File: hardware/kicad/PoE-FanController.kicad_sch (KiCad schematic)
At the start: 31 parts, among them J2 FAN1, J3 FAN2, J4 FAN3, J5 FAN4, J6 Molex_KK254_3pin, J8 Waveshare_ESP32P4POEETH, U1 LM2587-12

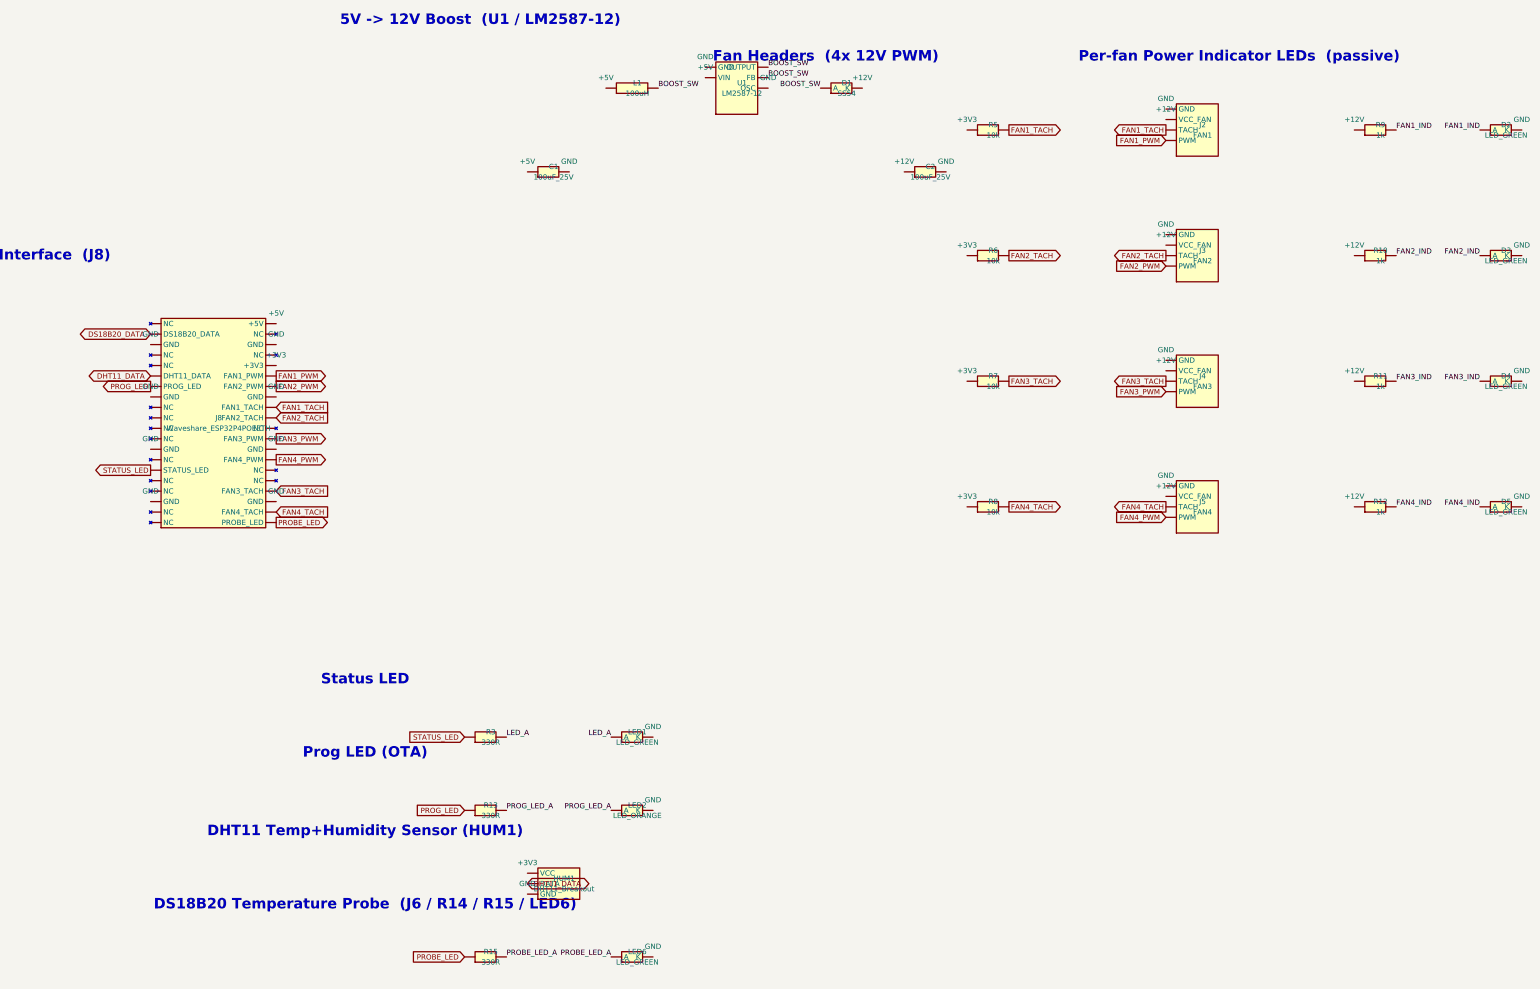
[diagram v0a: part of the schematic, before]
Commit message: hw(sch): overhaul pin assignments and rename signals per user spec
Signal changes (v0.6):
  Left column (all sensors/indicators now on left):
  - Pin 6  DS18B20_DATA (GPIO2)  was: STATUS_LED
  - Pin 7  PROBE_LED    (GPIO3)  was: NC
  - Pin 14 DHT11_DATA  (GPIO15)  was: PROG_LED
  - Pin 16 PROG_LED    (GPIO17)  was: NC
  - Pin 17 PWR_LED     (GPIO18)  renamed from STATUS_LED, was NC
  - Pin 19 NC (was DS18B20_DATA/GPIO19)
  - Pin 15 NC (was DHT11_DATA/GPIO16)

  Right column (fan signals only):
  - Pin 21 FAN4_TACH  (GPIO48)   was: PROBE_LED
  - Pin 22 FAN4_PWM   (GPIO47)   was: FAN4_TACH
  - Pin 26 FAN3_TACH  (GPIO32)   was: NC (note: verify EMAC not active)
  - Pin 27 FAN3_PWM   (GPIO27)   was: FAN4_PWM
  - Pin 32 FAN2_PWM   (GPIO22)   was: FAN1_TACH
  - Pin 34 FAN1_TACH  (GPIO21)   was: FAN2_PWM
  - Pins 24,29,31,35 now NC (GPIO46,GPIO26,GPIO23,GPIO20 unused)

Fan header assignments:
  - J2 (FAN1): TACH only (no PWM — full speed), pull-up R5
  - J3 (FAN2): PWM only (no TACH monitoring), no pull-up
  - J4 (FAN3): PWM + TACH, pull-up R7
  - J5 (FAN4): PWM + TACH, pull-up R8
  - R6 removed (FAN2 has no TACH)

Schematic cleanup:
  - Removed per-fan passive indicator LEDs (D2-D5, R9-R12) — reduces noise
  - PROBE_LED circuit now adjacent to J6/DS18B20 section in schematic
  - PWR_LED (was STATUS_LED) clearly named and documented

ERC: 0 errors (54 pre-existing lib_symbol_mismatch warnings)

Co-authored-by: Copilot <223556219+Copilot@users.noreply.github.com>
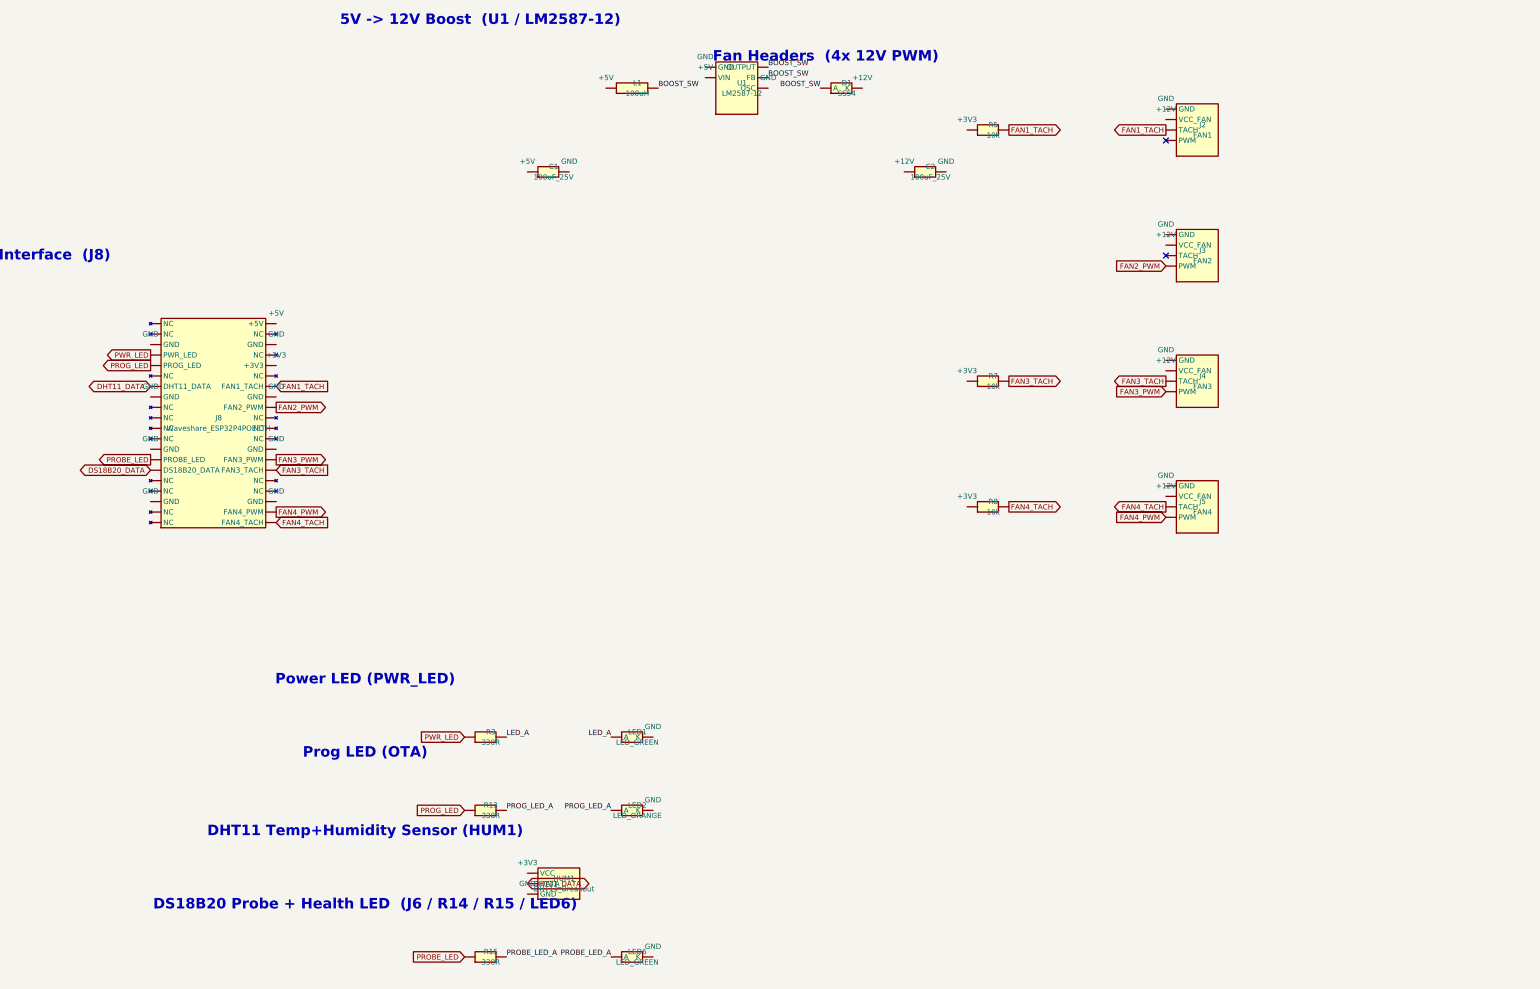
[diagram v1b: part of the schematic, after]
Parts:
- removed D3, D4, D5: LED_GREEN, LED_THT:LED_D3.0mm, symbol Custom:LED_SMD
- removed R10, R11, R12, R9: 1k, Resistor_THT:R_Axial_DIN0207_L6.3mm_D2.5mm_P7.62mm_Horizontal, symbol Custom:R
- removed R13: 330R, Resistor_THT:R_Axial_DIN0207_L6.3mm_D2.5mm_P7.62mm_Horizontal, symbol Custom:R
- removed R6: 10k, Resistor_THT:R_Axial_DIN0207_L6.3mm_D2.5mm_P7.62mm_Horizontal, symbol Custom:R
- R13: renamed from D2; value LED_GREEN -> 330R; footprint LED_THT:LED_D3.0mm -> Resistor_THT:R_Axial_DIN0207_L6.3mm_D2.5mm_P7.62mm_Horizontal; symbol Custom:LED_SMD -> Custom:R
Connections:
- net FAN1_IND is gone; now on net PROG_LED: R13.1
- net DHT11_DATA: now also J8.14 (DHT11_DATA); no longer J8.15 (DHT11_DATA)
- net DS18B20_DATA: now also J8.6 (DS18B20_DATA); no longer J8.19 (DS18B20_DATA)
- net FAN1_TACH: now also J8.34 (FAN1_TACH); no longer J8.32 (FAN1_TACH)
- net FAN2_PWM: now also J8.32 (FAN2_PWM); no longer J8.34 (FAN2_PWM)
- net FAN3_PWM: now also J8.27 (FAN3_PWM); no longer J8.29 (FAN3_PWM)
- net FAN3_TACH: now also J8.26 (FAN3_TACH); no longer J8.24 (FAN3_TACH)
- net FAN4_PWM: now also J8.22 (FAN4_PWM); no longer J8.27 (FAN4_PWM)
- net FAN4_TACH: now also J8.21 (FAN4_TACH); no longer J8.22 (FAN4_TACH)
- net PROBE_LED: now also J8.7 (PROBE_LED); no longer J8.21 (PROBE_LED)
- net PROG_LED: now also J8.16 (PROG_LED); no longer J8.14 (PROG_LED)
- net PROG_LED_A: now also R13.2
- net PWR_LED: now reaches J8.17 (PWR_LED)
- net PWR_LED: now also R3.1
- net FAN1_PWM: no longer names the net of J2.4 (PWM)
- net FAN1_PWM: no longer J8.35 (FAN1_PWM)
- net FAN2_TACH: no longer names the net of J3.3 (TACH)
- net FAN2_TACH: no longer J8.31 (FAN2_TACH)
- removed net STATUS_LED: J8.6 (STATUS_LED), R3.1
- no-connect marks 0 -> 2
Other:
- note added: "DS18B20 Probe + Health LED (J6 / R14 / R15 / LED6)"
- note added: "Power LED (PWR_LED)"
- note removed: "DS18B20 Temperature Probe (J6 / R14 / R15 / LED6)"
- note removed: "Per-fan Power Indicator LEDs (passive)"
- note removed: "Status LED"

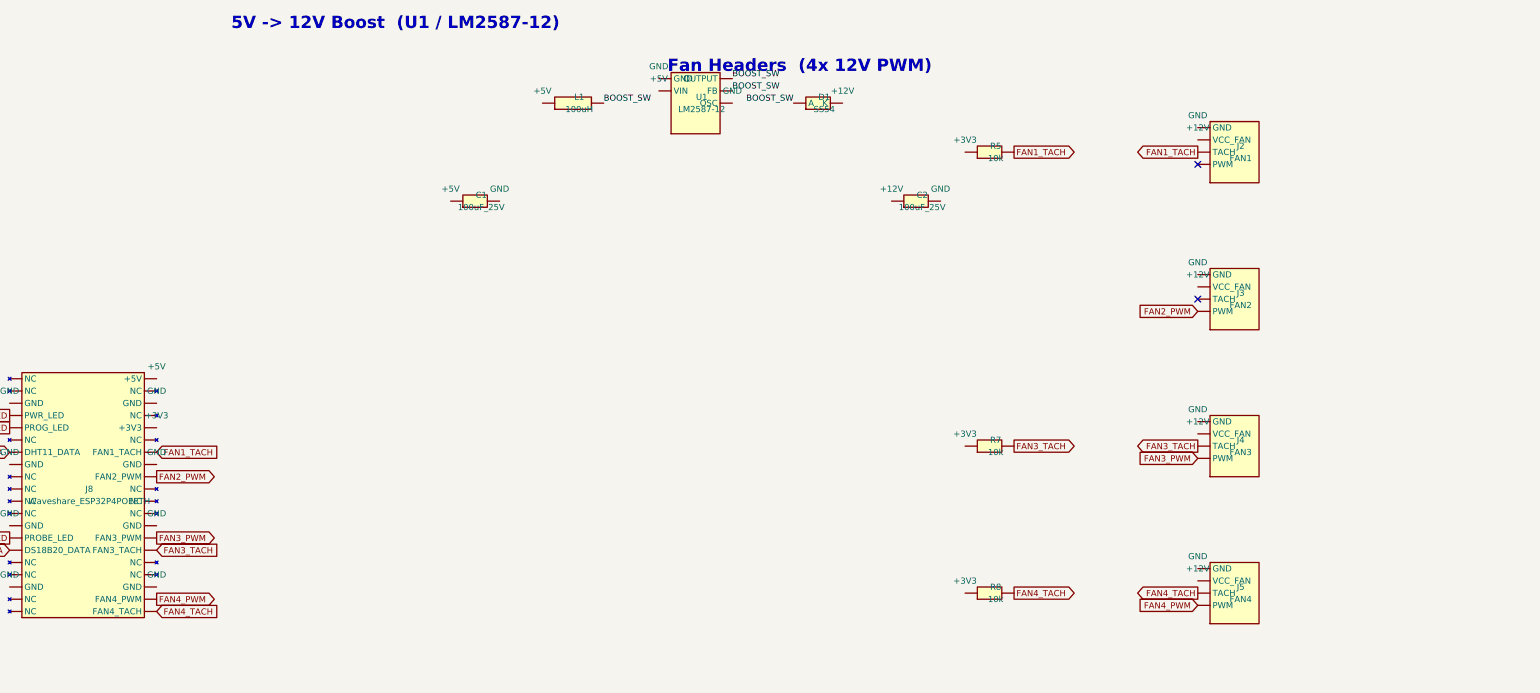
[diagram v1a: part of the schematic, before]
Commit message: hw(sch/pcb): add PWM-driven indicator LEDs (issue #175)
Schematic changes:
- FAN1_PWM re-added on J8 pin 35 (GPIO20) — all 4 fans now have PWM control
- fan_data updated: J2(FAN1_PWM+TACH), J3(FAN2_PWM only), J4/J5(PWM+TACH)
- 4x indicator LED circuits (D2-D5 + R9-R12, 150Ω) added to schematic
  Each LED tapped directly on FAN{n}_PWM signal line:
    FAN{n}_PWM ──[150Ω R]──[LED anode]──[LED cathode]── GND
  LED brightness proportional to PWM duty cycle
- Removed redundant R6 TACH pull-up (FAN2 has no TACH)
- ERC: 0 errors

PCB changes:
- D2-D5 (PWM LEDs) placed at (67, 10/22/34/46) — between J8 and fan headers
- R9-R12 (150Ω resistors) placed at (53, 10/22/34/46)
- R15 (PROBE_LED resistor) moved to (7,50) — left zone above J6
- LED6 (PROBE_LED) moved to (7,44) — directly above J6(DS18B20) as requested
- All pad nets synced to new schematic v0.6 + issue #175

Routing: 125 tracks. Complex DRC conflicts (TACH/+12V interactions, left-zone
signal routing through ESP32 zone) require KiCad GUI for final cleanup.
8 unconnected items and routing shorts need interactive routing session.

Closes #175

Co-authored-by: Copilot <223556219+Copilot@users.noreply.github.com>
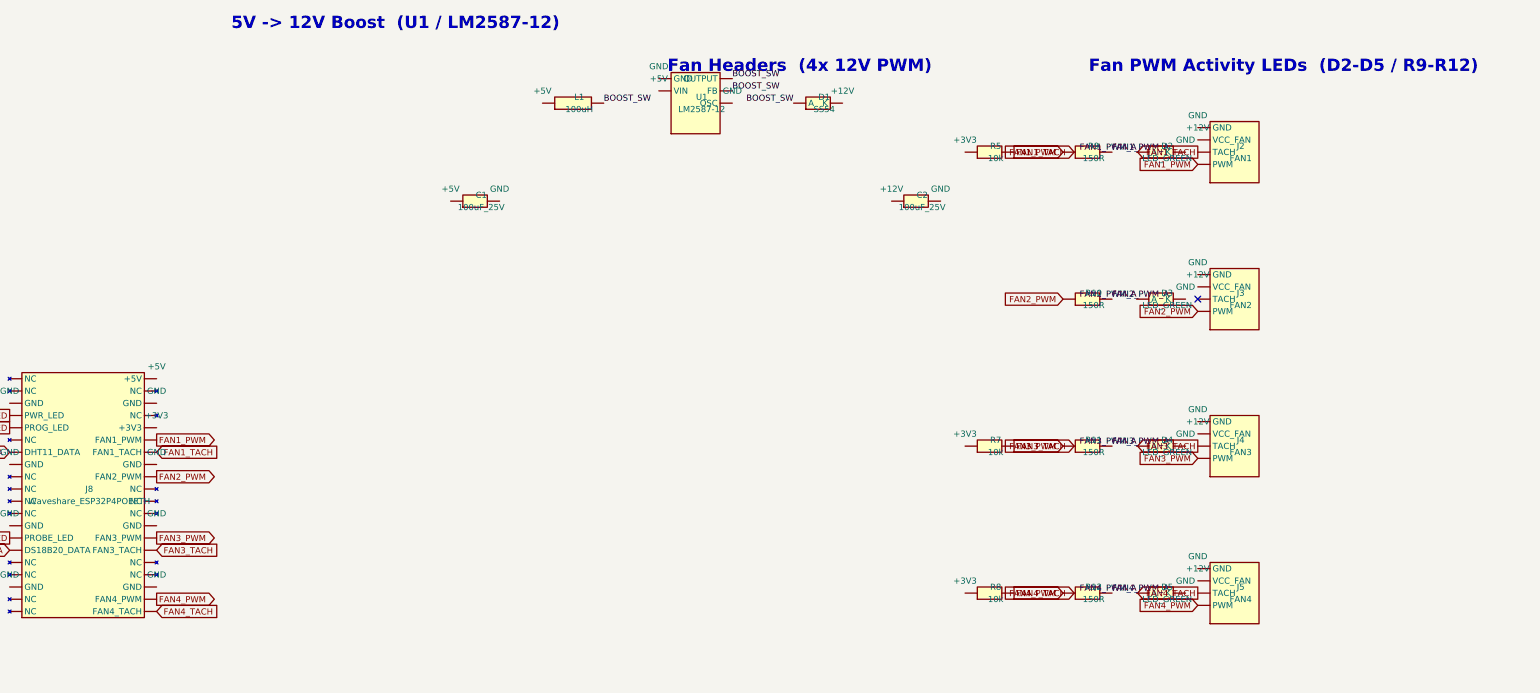
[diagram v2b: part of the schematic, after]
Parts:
- removed LED6: LED_GREEN, LED_THT:LED_D3.0mm, symbol Custom:LED
- added D3, D4, D5, LED1: LED_GREEN, LED_THT:LED_D3.0mm, symbol Custom:LED
- added J8: Waveshare_ESP32P4POEETH, Custom:ESP32-P4-PoE-ETH-PinSocket, symbol Custom:J8_Waveshare
- added R10, R11, R12: 150R, Resistor_THT:R_Axial_DIN0207_L6.3mm_D2.5mm_P7.62mm_Horizontal, symbol Custom:R
- added R3: 330R, Resistor_THT:R_Axial_DIN0207_L6.3mm_D2.5mm_P7.62mm_Horizontal, symbol Custom:R
- LED6: renamed from J8; value Waveshare_ESP32P4POEETH -> LED_GREEN; footprint Custom:ESP32-P4-PoE-ETH-PinSocket -> LED_THT:LED_D3.0mm; symbol Custom:J8_Waveshare -> Custom:LED
- R9: renamed from R3; value 330R -> 150R
- renumbered LED1 to D2
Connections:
- net DHT11_DATA: now also J8.14 (DHT11_DATA); no longer LED6.14 (DHT11_DATA)
- net DS18B20_DATA: now also J8.6 (DS18B20_DATA); no longer LED6.6 (DS18B20_DATA)
- net FAN1_TACH: now also J8.34 (FAN1_TACH); no longer LED6.34 (FAN1_TACH)
- net FAN2_PWM: now also J8.32 (FAN2_PWM), R10.1; no longer LED6.32 (FAN2_PWM)
- net FAN3_PWM: now also J8.27 (FAN3_PWM), R11.1; no longer LED6.27 (FAN3_PWM)
- net FAN3_TACH: now also J8.26 (FAN3_TACH); no longer LED6.26 (FAN3_TACH)
- net FAN4_PWM: now also J8.22 (FAN4_PWM), R12.1; no longer LED6.22 (FAN4_PWM)
- net FAN4_TACH: now also J8.21 (FAN4_TACH); no longer LED6.21 (FAN4_TACH)
- net LED_A: now also LED1.1 (A), R3.2; no longer D2.1 (A), R9.2
- net PROBE_LED: now also J8.7 (PROBE_LED); no longer LED6.7 (PROBE_LED)
- net PROBE_LED_A: now also LED6.1 (A)
- net PROG_LED: now also J8.16 (PROG_LED); no longer LED6.16 (PROG_LED)
- net PWR_LED: now also J8.17 (PWR_LED), R3.1; no longer LED6.17 (PWR_LED), R9.1
- net FAN1_PWM: now reaches J2.4 (PWM)
- net FAN1_PWM: now also R9.1, J8.35 (FAN1_PWM)
- new net FAN1_PWM_A: D2.1 (A), R9.2
- new net FAN2_PWM_A: D3.1 (A), R10.2
- new net FAN3_PWM_A: D4.1 (A), R11.2
- new net FAN4_PWM_A: D5.1 (A), R12.2
- no-connect marks 2 -> 1
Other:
- note added: "Fan PWM Activity LEDs (D2-D5 / R9-R12)"
- moved on the sheet: D2, R9

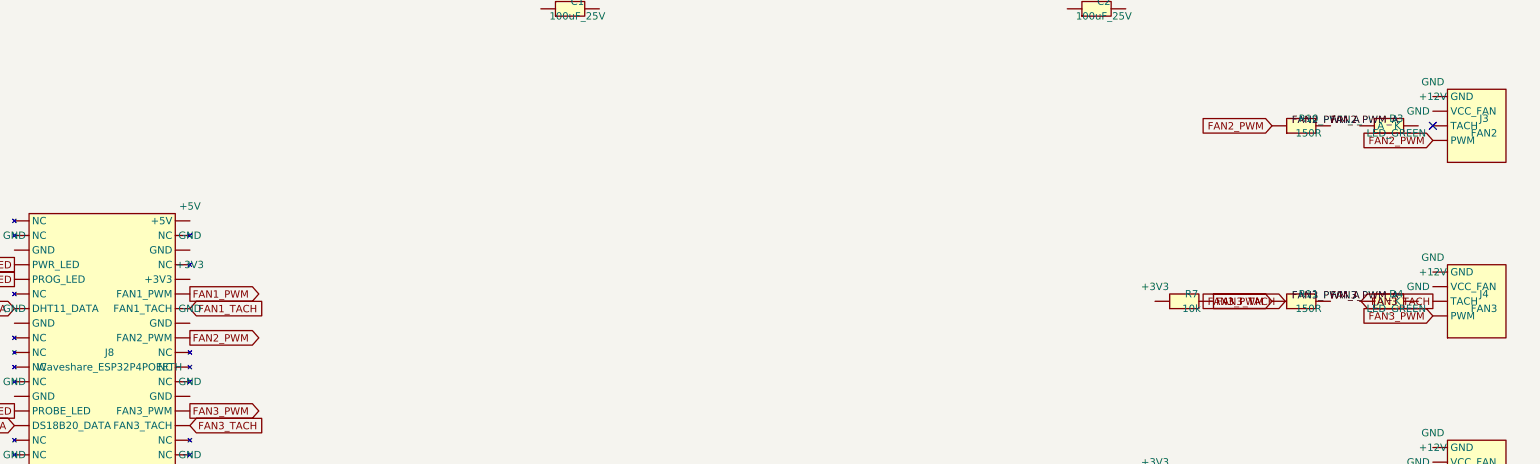
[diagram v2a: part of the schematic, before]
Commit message: hw(sch/pcb): restore R6 FAN2_TACH pull-up; assign GPIO23 to J8 pin 31
- J8 pin 31 (GPIO23): FAN2_TACH (was NC)
- R6 (10kΩ): pull-up from FAN2_TACH to +3V3, placed at (46,28) — same column as R5/R7/R8
- fan_data updated: J3 now has FAN2_PWM + FAN2_TACH (full control + monitoring)
- All 4 fan headers (J2-J5) now have both PWM and TACH signals
- ERC: 0 errors

Co-authored-by: Copilot <223556219+Copilot@users.noreply.github.com>
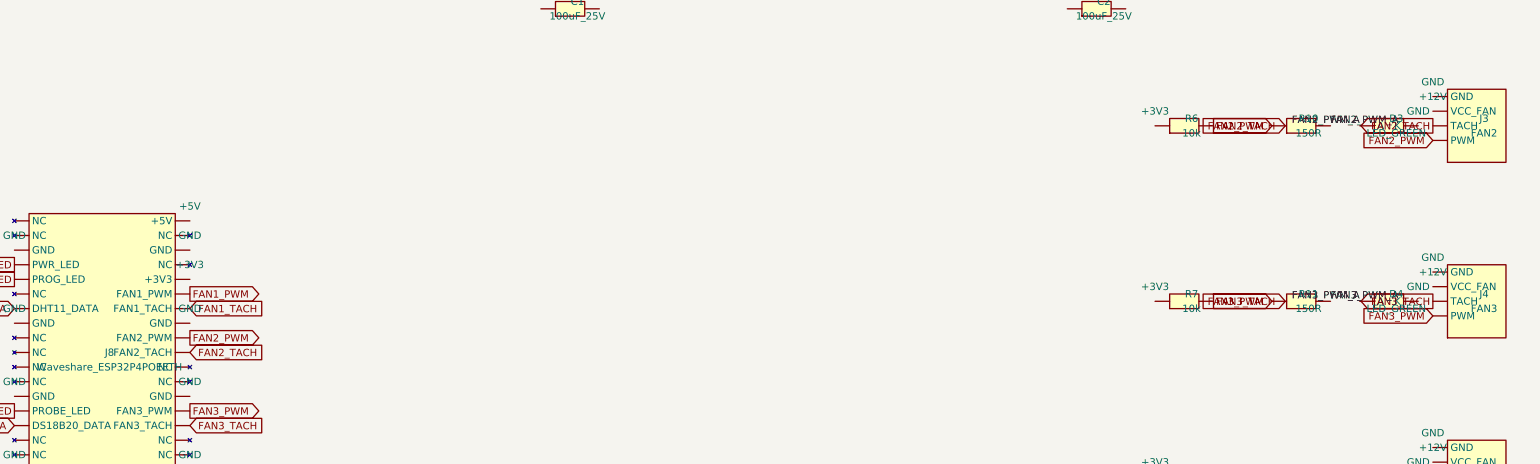
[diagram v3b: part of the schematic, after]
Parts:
- removed D2, D3, D4: LED_GREEN, LED_THT:LED_D3.0mm, symbol Custom:LED
- added R10, R11, R12: 150R, Resistor_THT:R_Axial_DIN0207_L6.3mm_D2.5mm_P7.62mm_Horizontal, symbol Custom:R
- added R6: 10k, Resistor_THT:R_Axial_DIN0207_L6.3mm_D2.5mm_P7.62mm_Horizontal, symbol Custom:R
- D2: renamed from R10; value 150R -> LED_GREEN; footprint Resistor_THT:R_Axial_DIN0207_L6.3mm_D2.5mm_P7.62mm_Horizontal -> LED_THT:LED_D3.0mm; symbol Custom:R -> Custom:LED
- D3: renamed from R11; value 150R -> LED_GREEN; footprint Resistor_THT:R_Axial_DIN0207_L6.3mm_D2.5mm_P7.62mm_Horizontal -> LED_THT:LED_D3.0mm; symbol Custom:R -> Custom:LED
- D4: renamed from R12; value 150R -> LED_GREEN; footprint Resistor_THT:R_Axial_DIN0207_L6.3mm_D2.5mm_P7.62mm_Horizontal -> LED_THT:LED_D3.0mm; symbol Custom:R -> Custom:LED
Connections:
- net FAN1_PWM_A: now also D2.1 (A)
- net FAN2_PWM: now also R10.1; no longer D2.1
- net FAN2_PWM_A: now also D3.1 (A), R10.2; no longer D2.2
- net FAN3_PWM: now also R11.1; no longer D3.1
- net FAN3_PWM_A: now also D4.1 (A), R11.2; no longer D3.2
- net FAN4_PWM: now also R12.1; no longer D4.1
- net FAN4_PWM_A: now also R12.2; no longer D4.2
- net FAN2_TACH: now reaches J3.3 (TACH)
- net FAN2_TACH: now also J8.31 (FAN2_TACH), R6.2
- no-connect marks 1 -> 0
